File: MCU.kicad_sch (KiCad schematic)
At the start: 69 parts, among them IC1 MT2492, J1 FH34SRJ-8S-0.5SH_50_, U1 TEENSY 4.0, U2 ESP32-C3-MINI-1-H4X, U3 TLV75733PDBV

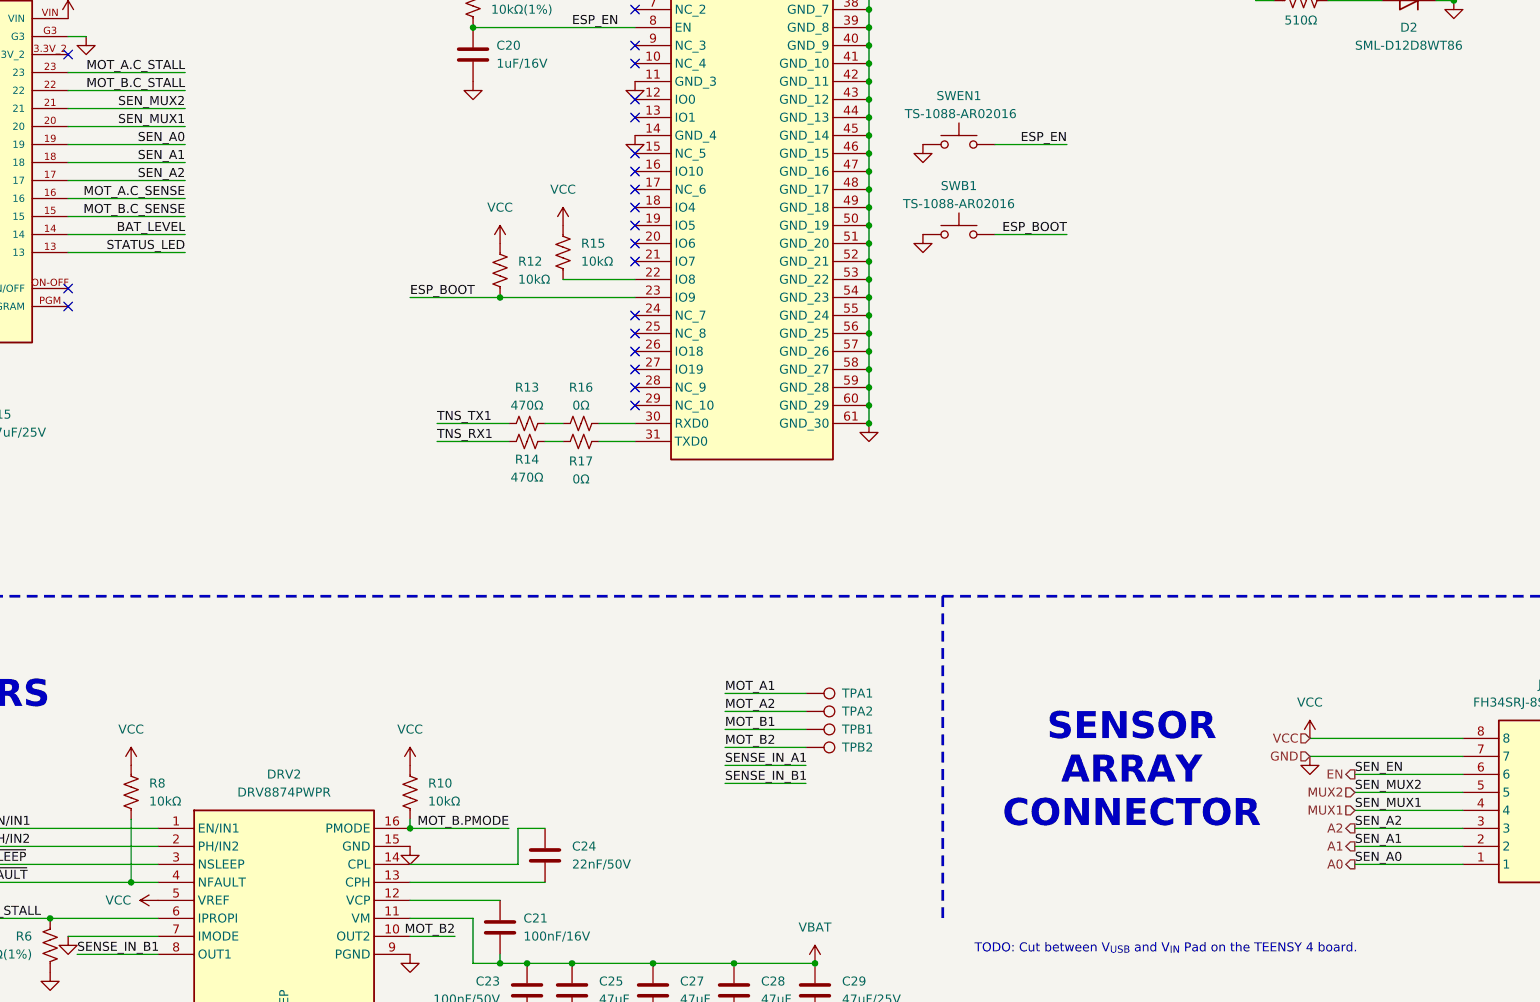
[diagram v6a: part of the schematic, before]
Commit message: Added 3D models to third party footprints. Final Teensy version, switching to SAMD51 custom setup. Please add tag.
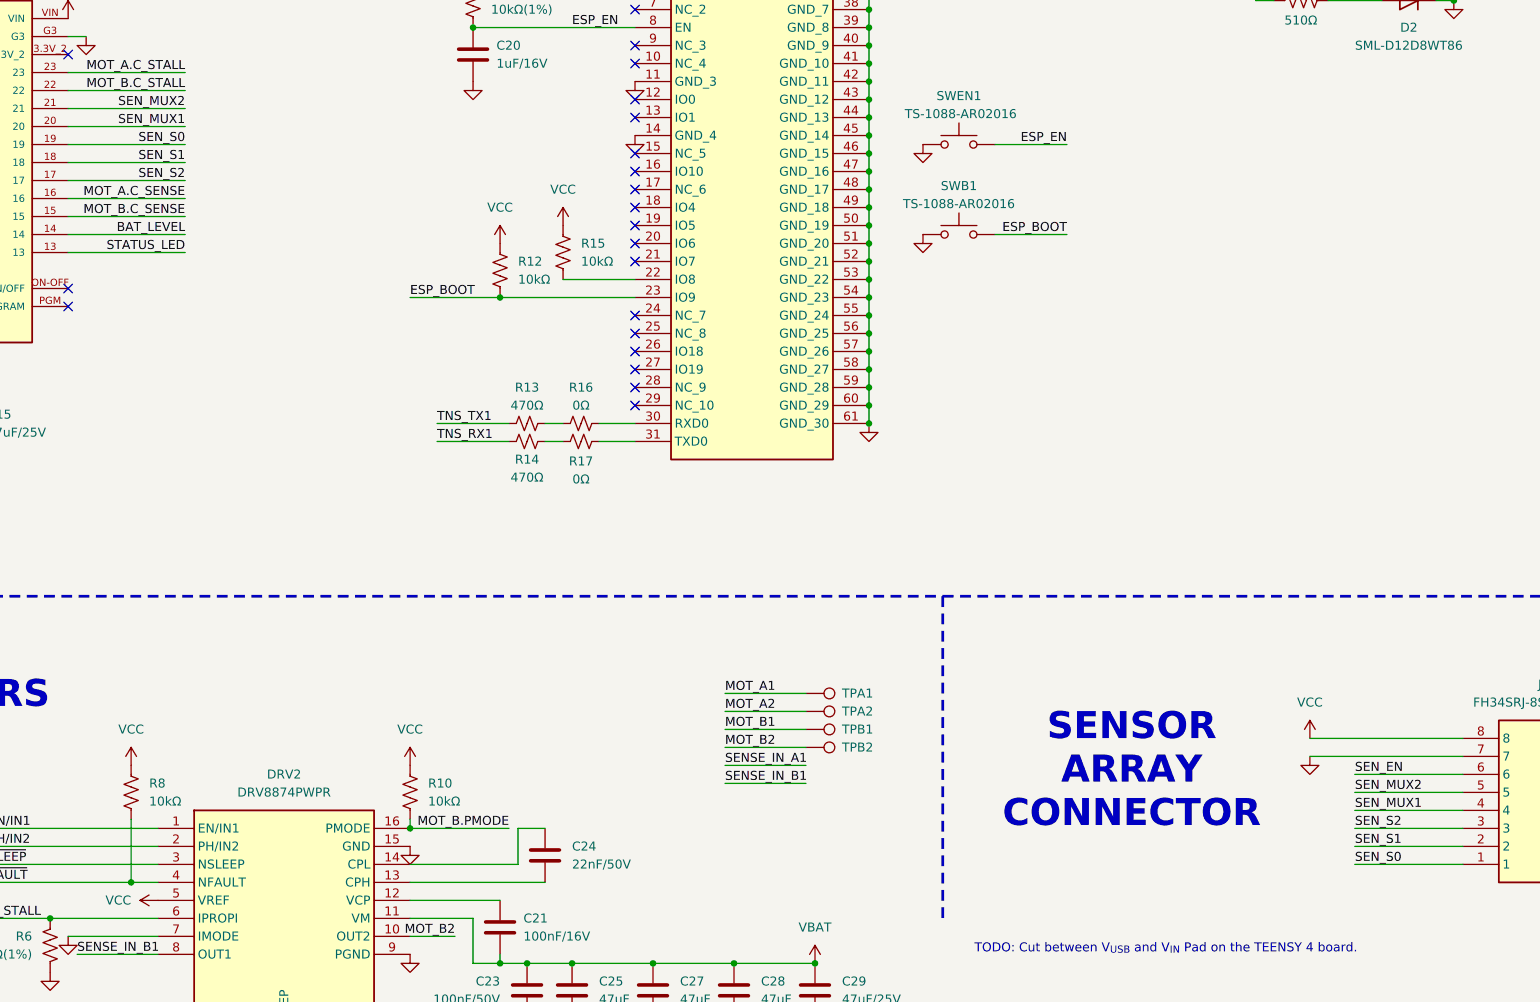
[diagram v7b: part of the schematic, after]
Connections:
- net A0 renamed SEN_S0
- net A1 renamed SEN_S1
- net A2 renamed SEN_S2
- net EN renamed SEN_EN
- net MUX1 renamed SEN_MUX1
- net MUX2 renamed SEN_MUX2
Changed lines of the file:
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@@
 		)
 	)
-	(label "SEN_A2"
+	(label "SEN_S2"
 		(at 358.14 240.03 0)
 		(effects
@@
 		)
 	)
-	(label "SEN_A0"
+	(label "SEN_S0"
 		(at 358.14 245.11 0)
 		(effects
@@
 		)
 	)
-	(label "SEN_A0"
+	(label "SEN_S0"
 		(at 193.04 143.51 180)
 		(effects
@@
 		)
 	)
-	(label "SEN_A1"
+	(label "SEN_S1"
 		(at 358.14 242.57 0)
 		(effects
@@
 		)
 	)
-	(label "SEN_A1"
+	(label "SEN_S1"
 		(at 193.04 146.05 180)
 		(effects
@@
 		)
 	)
-	(label "SEN_A2"
+	(label "SEN_S2"
 		(at 193.04 148.59 180)
 		(effects
@@
 		)
 	)
-	(hierarchical_label "GND"
-		(shape input)
-		(at 351.79 229.87 180)
-		(effects
-			(font
-				(size 1.27 1.27)
-			)
-			(justify right)
-		)
-	)
-	(hierarchical_label "EN"
-		(shape output)
-		(at 358.14 232.41 180)
-		(effects
-			(font
-				(size 1.27 1.27)
-			)
-			(justify right)
-		)
-	)
-	(hierarchical_label "VCC"
-		(shape input)
-		(at 351.79 227.33 180)
-		(effects
-			(font
-				(size 1.27 1.27)
-			)
-			(justify right)
-		)
-	)
-	(hierarchical_label "A2"
-		(shape output)
-		(at 358.14 240.03 180)
-		(effects
-			(font
-				(size 1.27 1.27)
-			)
-			(justify right)
-		)
-	)
-	(hierarchical_label "A1"
-		(shape output)
-		(at 358.14 242.57 180)
-		(effects
-			(font
-				(size 1.27 1.27)
-			)
-			(justify right)
-		)
-	)
-	(hierarchical_label "MUX2"
-		(shape input)
-		(at 358.14 234.95 180)
-		(effects
-			(font
-				(size 1.27 1.27)
-			)
-			(justify right)
-		)
-	)
-	(hierarchical_label "MUX1"
-		(shape input)
-		(at 358.14 237.49 180)
-		(effects
-			(font
-				(size 1.27 1.27)
-			)
-			(justify right)
-		)
-	)
-	(hierarchical_label "A0"
-		(shape output)
-		(at 358.14 245.11 180)
-		(effects
-			(font
-				(size 1.27 1.27)
-			)
-			(justify right)
-		)
-	)
 	(rule_area
 		(exclude_from_sim no)
@@
 	)
 	(symbol
+		(lib_id "power:GND")
+		(at 351.79 229.87 0)
+		(unit 1)
+		(body_style 1)
+		(exclude_from_sim no)
+		(in_bom yes)
+		(on_board yes)
+		(in_pos_files yes)
+		(dnp no)
+		(fields_autoplaced yes)
+		(property "Reference" "#PWR058"
+			(at 351.79 236.22 0)
+			(hide yes)
+			(show_name no)
+			(do_not_autoplace no)
+			(effects
+				(font
+					(size 1.27 1.27)
+				)
+			)
+		)
+		(property "Value" "GND"
+			(at 351.79 234.95 0)
+			(hide yes)
+			(show_name no)
+			(do_not_autoplace no)
+			(effects
+				(font
+					(size 1.27 1.27)
+				)
+			)
+		)
+		(property "Footprint" ""
+			(at 351.79 229.87 0)
+			(hide yes)
+			(show_name no)
+			(do_not_autoplace no)
+			(effects
+				(font
+					(size 1.27 1.27)
+				)
+			)
+		)
+		(property "Datasheet" ""
+			(at 351.79 229.87 0)
+			(hide yes)
+			(show_name no)
+			(do_not_autoplace no)
+			(effects
+				(font
+					(size 1.27 1.27)
+				)
+			)
+		)
+		(property "Description" "Power symbol creates a global label with name \"GND\" , ground"
+			(at 351.79 229.87 0)
+			(hide yes)
+			(show_name no)
+			(do_not_autoplace no)
+			(effects
+				(font
+					(size 1.27 1.27)
+				)
+			)
+		)
+		(pin "1"
+		)
+		(instances
+			(project "SAVITAR_V2"
+				(path "/f6d97783-3721-4b78-8f0f-ed81f34e7161/c16c02dc-523d-461d-bb67-ac432d665908"
+					(reference "#PWR058")
+					(unit 1)
+				)
+			)
+		)
+	)
+	(symbol
 		(lib_id "Device:C")
 		(at 250.19 45.72 180)
@@
 					(unit 1)
 				)
-			)
-		)
-	)
-	(symbol
-		(lib_id "power:GND")
-		(at 351.79 229.87 0)
-		(mirror y)
-		(unit 1)
-		(body_style 1)
-		(exclude_from_sim no)
-		(in_bom yes)
-		(on_board yes)
-		(in_pos_files yes)
-		(dnp no)
-		(fields_autoplaced yes)
-		(property "Reference" "#PWR058"
-			(at 351.79 236.22 0)
-			(hide yes)
-			(show_name no)
-			(do_not_autoplace no)
-			(effects
-				(font
-					(size 1.27 1.27)
-				)
-			)
-		)
-		(property "Value" "GND"
-			(at 351.79 234.95 0)
-			(hide yes)
-			(show_name no)
-			(do_not_autoplace no)
-			(effects
-				(font
-					(size 1.27 1.27)
-				)
-			)
-		)
-		(property "Footprint" ""
-			(at 351.79 229.87 0)
-			(hide yes)
-			(show_name no)
-			(do_not_autoplace no)
-			(effects
-				(font
-					(size 1.27 1.27)
-				)
-			)
-		)
-		(property "Datasheet" ""
-			(at 351.79 229.87 0)
-			(hide yes)
-			(show_name no)
-			(do_not_autoplace no)
-			(effects
-				(font
-					(size 1.27 1.27)
-				)
-			)
-		)
-		(property "Description" "Power symbol creates a global label with name \"GND\" , ground"
-			(at 351.79 229.87 0)
-			(hide yes)
-			(show_name no)
-			(do_not_autoplace no)
-			(effects
-				(font
-					(size 1.27 1.27)
-				)
-			)
-		)
-		(pin "1"
-		)
-		(instances
-			(project "MCU"
-				(path "/b713d384-4380-4aef-98de-8773eb5f4cc6"
-					(reference "#PWR051")
-					(unit 1)
-				)
-			)
-			(project "SAVITAR_V2"
-				(path "/f6d97783-3721-4b78-8f0f-ed81f34e7161/c16c02dc-523d-461d-bb67-ac432d665908"
-					(reference "#PWR058")
-					(unit 1)
-				)

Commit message: Add main board: power tree, USB-C, ESP32-C3, dual DRV8874 motor drive
Power:
- Add 100nF per-pin decoupling + 22uF bulk on SAMD51 supplies
- Add 120R@100MHz/2A ferrite bead on VDDANA for ADC supply isolation
- Change buck output 5V -> 3.8V; inductor 22uH -> 6.8uH; FB R7 13.7k -> 18.7k
- Add 22pF feedforward cap across buck FB top resistor
- Keep TLV75733 LDO (fed from 3.8V) for 3.3V rail; dissipation now ~0.15W

USB:
- Add USBLC6-2SC6 ESD protection on D+/D-/VBUS
- Isolate VBUS from power path (sense-only); board powered from battery

ESP32-C3-MINI-1:
- Change 3V3 bulk 1x22uF -> 2x22uF for 350mA TX bursts
- 10k EN + 1uF (10ms POR), boot/reset buttons to GND
- UART0 to SAMD51 for data; native USB-Serial-JTAG on GPIO18/19 available

Motor drive (x2, DRV8874):
- VREF tied to VCC: fixed ~2.5A ITRIP, no overcurrent shutdown (uptime)
- IMODE=GND, PMODE=VCC (PWM mode); 22nF CPL/CPH, 100nF VCP-VM, 4x47uF+100nF VM bulk
- Add INA240A1 + 50mohm 1206 shunt per motor as commutation-ripple pseudo-encoder

TODO: 2S over-discharge cutoff, crystal load caps 15pF -> 18pF, ESP program path, sensor array
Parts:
- removed R9: 100kΩ(1%), Resistor_SMD:R_0603_1608Metric, symbol Device:R_US
- added C33, C34: 18pF/25V, Capacitor_SMD:C_0603_1608Metric, symbol Device:C
- added C35: 1uF/16V, Capacitor_SMD:C_0603_1608Metric, symbol Device:C
- added C36: 1uF (X7R), Capacitor_SMD:C_0603_1608Metric, symbol Device:C
- added C41: 10uF (X7R), Capacitor_SMD:C_0603_1608Metric, symbol Device:C
- added C42: 100nF (X7R), Capacitor_SMD:C_0603_1608Metric, symbol Device:C
- added C43, C44, C45, C46: 100nF, Capacitor_SMD:C_0603_1608Metric, symbol Device:C
- added C47: 22uF/25V, Capacitor_SMD:C_0805_2012Metric, symbol Device:C
- added C48: 22pF, Capacitor_SMD:C_0603_1608Metric, symbol Device:C
- added C49: 22uF/25V, Capacitor_SMD:C_1206_3216Metric, symbol Device:C
- added FB1: 50mΩ 2A, Inductor_SMD:L_0603_1608Metric, symbol Device:FerriteBead
- added J3: USB_C_Receptacle_USB2.0_16P, symbol Connector:USB_C_Receptacle_USB2.0_16P
- added R30: 10kΩ(1%), Resistor_SMD:R_0603_1608Metric, symbol Device:R_US
- added R31: 10kΩ, Resistor_SMD:R_0603_1608Metric, symbol Device:R_US
- added R34: 330Ω, Resistor_SMD:R_0603_1608Metric, symbol Device:R_Small_US
- added R37: 100kΩ(1%), Resistor_SMD:R_0603_1608Metric, symbol Device:R_US
- added R39, R40: 5.1kΩ, Resistor_SMD:R_0603_1608Metric, symbol Device:R_US
- added SW3: TS-1088-AR02016, Button_Switch_SMD:SW_SPST_TS-1088-xR020, symbol Switch:SW_Push
- added TPA3, TPA4, TPA5, TPA6, TPA7: TestPoint, TestPoint:TestPoint_THTPad_D2.0mm_Drill1.0mm, symbol Connector:TestPoint
- added U20: ATSAMD51J19A-A, Package_QFP:TQFP-64_10x10mm_P0.5mm, symbol MCU_Microchip_SAMD:ATSAMD51J19A-A
- added U21: USBLC6-2SC6, Package_TO_SOT_SMD:SOT-23-6, symbol Power_Protection:USBLC6-2SC6
- added Y1: 32.768kHz, symbol Device:Crystal
- L1: value 22uH -> 6.8uH
- R7: value 13.7kΩ(1%) -> 18.7kΩ(1%)
- SHUNT1, SHUNT2: value 33mΩ -> 50mΩ
- renumbered SWEN1 to SW1, SWB1 to SW2
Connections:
- net +5V: no longer C17.1, C19.2, C26.2, L1.2, U3.1 (IN), U3.3 (EN)
- net GND: now also C33.2, C34.2, C35.1, C36.2, C41.2, C42.1, C43.1, C44.1, C45.1, C46.1, C47.2, C49.2, J3.A1 (GND), J3.A12 (GND), J3.B1 (GND), J3.B12 (GND), J3.SH (SHIELD), R39.1, R40.1, SW3.1, TPA6.1, U20.22 (GND), U20.33 (GND), U20.47 (GND), U20.54 (GND), U20.7 (GNDANA), U21.2 (GND)
- net TNS_RX1: no longer R14.1
- net TNS_TX1: no longer R13.1
- net VCC: now also C42.2, C43.2, C44.2, C45.2, C46.2, C47.1, C49.1, FB1.1, R30.1, R31.1, U20.21 (VDDIOB), U20.34 (VDDIO), U20.48 (VDDIO), U20.56 (VDDIO)
- net at IC1.3 (FB), R7.1: now also C48.1, R37.2
- net ESP_BOOT: no longer names the net of R12.2, SW2.2, U2.23 (IO9)
- new net: R34.1, SW3.2
- new net: C35.2, R30.2, R34.2, TPA5.1, U20.52 (~{RESET})
- new net: C34.1, U20.2 (PA01), Y1.1
- new net: J3.A7 (D-), J3.B7 (D-), U21.1 (I/O1)
- new net: J3.A6 (D+), J3.B6 (D+), U21.3 (I/O2)
- new net: C36.1, C41.1, U20.53 (VDDCORE)
- new net: C33.1, U20.1 (PA00), Y1.2
- new net: J3.B5 (CC2), R40.2
- new net: J3.A5 (CC1), R39.2
- new net: FB1.2, TPA7.1, U20.8 (VDDANA)
- new net +3V8: C17.1, C19.2, C26.2, C48.2, L1.2, R37.1, U3.1 (IN), U3.3 (EN)
- new net D+: U20.46 (PA25), U21.4 (I/O2)
- new net D-: U20.45 (PA24), U21.6 (I/O1)
- new net SAMD_RX1: R14.1
- new net SAMD_TX1: R13.1
- new net SWCLK: R31.2, TPA3.1, U20.57 (PA30)
- new net SWDIO: TPA4.1, U20.58 (PA31)
- new net VBUS: J3.A4 (VBUS), J3.A9 (VBUS), J3.B4 (VBUS), J3.B9 (VBUS), U21.5 (VBUS)
- no-connect marks 32 -> 35
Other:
- note added: "SAMD51"
- note added: "TX Peak 350mA @ 20dBm transmission"
- note added: "USB 2.0"
- note removed: "∆V_{OUT} = 4mV"
- moved on the sheet: C10, C12, C13, C15, C16, C17, C18, C19, C20, C22, C26, C30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
